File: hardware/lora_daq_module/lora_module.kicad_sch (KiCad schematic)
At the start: 28 parts, among them J2 SMA_Edge_50Ω, J3 USB_C_Receptacle_USB2.0_14P, J4 EXT_UART, J5 SWD, J6 Micro_SD_Card_Det1, U3 CP2102N-Axx-xQFN20, U4 Wio-E5_STM32WLE5JC, U5 CAT24C256

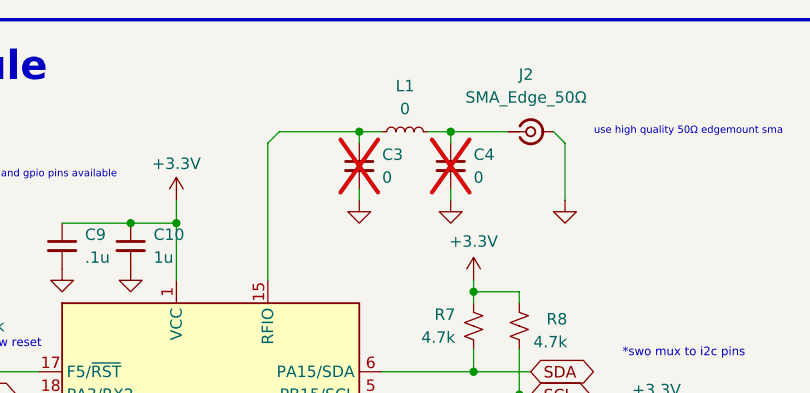
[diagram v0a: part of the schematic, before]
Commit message: assign parts and update BOM in symbol field table, warn: pcb footprints need update
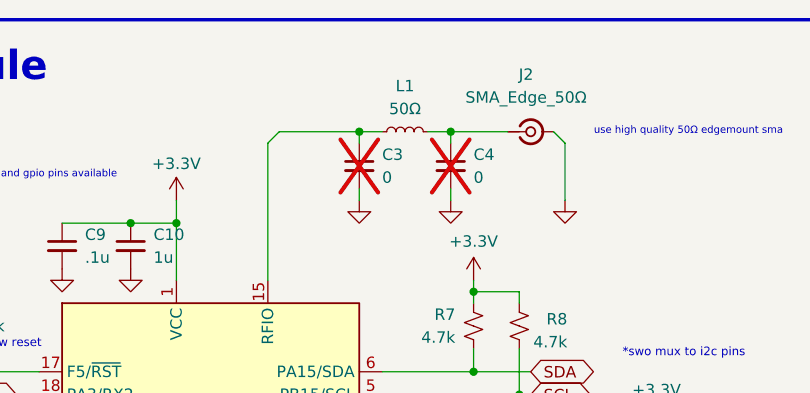
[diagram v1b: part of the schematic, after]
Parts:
- C10, C5: Desc (none) -> CAP CER 1UF 16V X7R 0603; Dist (none) -> Digikey; Dist PN (none) -> 490-5241-1-ND; Mfr (none) -> Murata Electronics; Mfr PN (none) -> GCM188R71C105KA64D
- C11, C13: Desc (none) -> CAP CER 10000PF 100V X7R 0603; Dist (none) -> Digikey; Dist PN (none) -> 490-4781-1-ND; Mfr (none) -> Murata Electronics; Mfr PN (none) -> GCM188R72A103KA37D
- C12, C6, C7, C9: Desc (none) -> CAP CER 0.1UF 16V X7R 0603; Dist (none) -> Digikey; Dist PN (none) -> 311-1088-1-ND; Mfr (none) -> YAGEO; Mfr PN (none) -> CC0603KRX7R7BB104
- D3: Desc (none) -> TVS DIODE 5.5VWM 8.5VC SOT1434; Dist (none) -> Digikey; Dist PN (none) -> F2715CT-ND; Mfr (none) -> Littelfuse Inc.; Mfr PN (none) -> SP0503BAHTG
- J2: Desc (none) -> SMA Connector Jack, Female Socket 50 Ohms Board Edge, End L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; Dist (none) -> Digkey; Dist PN (none) -> 900-0732511153-ND; Mfr (none) -> Molex; Mfr PN (none) -> 0732511153
- J3: Desc (none) -> CONN RCP USB3.1 TYPEC 24P SMD RA; Dist (none) -> Digikey; Dist PN (none) -> WM12856CT-ND; Mfr (none) -> Molex; Mfr PN (none) -> 1054500101
- J4: Desc (none) -> Connector Header Through Hole 3 position 0.098" (2.50mm); Dist (none) -> Digikey; Dist PN (none) -> 455-B3B-EH-A-ND; Mfr (none) -> JST Sales America Inc.; Mfr PN (none) -> B3B-EH-A
- J5: Desc (none) -> CONN HEADER VERT 6POS 2.54MM; Dist (none) -> Digikey; Dist PN (none) -> 732-5295-ND; Mfr (none) -> Würth Elektronik; Mfr PN (none) -> 61300621121
- J6: Desc (none) -> CONN MICRO SD CARD R/A SMD; Dist (none) -> Digikey; Dist PN (none) -> WM6357CT-ND; Mfr (none) -> Molex; Mfr PN (none) -> 1040310811
- L1: value 0 -> 50Ω; Desc (none) -> 50 Ohms ±0.1% 0.52W Chip Resistor 1206 (3216 Metric) Anti-S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; Dist (none) -> Digikey; Dist PN (none) -> 541-TNPW120650R0BEENCT-ND; Mfr (none) -> Vishay Dale; Mfr PN (none) -> TNPW120650R0BEEN
- R4, R5: Desc (none) -> 5.1 kOhms ±1% 0.1W, 1/10W Chip Resistor 0603 (1608 Metric) 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; Dist (none) -> Digikey; Dist PN (none) -> 311-5.10KHRCT-ND; Mfr (none) -> YAGEO; Mfr PN (none) -> RC0603FR-075K1L
- R6, R7, R8, R9: Desc (none) -> 4.7 kOhms ±5% 0.1W, 1/10W Chip Resistor 0603 (1608 Metric) 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; Dist (none) -> Digikey; Dist PN (none) -> 311-4.7KGRCT-ND; Mfr (none) -> YAGEO; Mfr PN (none) -> RC0603JR-074K7L
- TP1: now left out of the parts list
- U3: Desc (none) -> IC USB TO UART BRIDGE QFN20; Dist (none) -> Digikey; Dist PN (none) -> 336-5886-1-ND; Mfr (none) -> Silicon Labs; Mfr PN (none) -> CP2102N-A02-GQFN20R
- U4: Desc (none) -> RF TXRX MOD ISM<1GHZ SMD LORA; Dist (none) -> Digikey; Dist PN (none) -> 1597-317990829CT-ND; Mfr (none) -> Seeed Technology Co., Ltd; Mfr PN (none) -> 317990829
- U5: Desc (none) -> EEPROM Memory IC 256Kbit I2C 1 MHz 500 ns 8-SOIC; Dist (none) -> Digikey; Dist PN (none) -> CAT24C256WI-GT3OSCT-ND; Mfr (none) -> onsemi; Mfr PN (none) -> CAT24C256WI-GT3

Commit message: near-complete layout of power domain
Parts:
- J3: footprint Connector_USB:USB_C_Receptacle_Molex_105450-0101 -> Connector_USB:USB_C_Receptacle_GCT_USB4105-xx-A_16P_TopMnt_Horizontal; Desc CONN RCP USB3.1 TYPEC 24P SMD RA -> USB-C (USB TYPE-C) USB 2.0 Receptacle Connector 24 (16+8 Du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; Dist PN WM12856CT-ND -> 2073-USB4105-GF-A-120CT-ND; Mfr Molex -> GCT; Mfr PN 1054500101 -> USB4105-GF-A-120
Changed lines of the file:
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@@
 			)
 		)
-		(property "Footprint" "Connector_USB:USB_C_Receptacle_Molex_105450-0101"
+		(property "Footprint" "Connector_USB:USB_C_Receptacle_GCT_USB4105-xx-A_16P_TopMnt_Horizontal"
 			(at 39.37 54.61 0)
 			(effects
@@
 			)
 		)
-		(property "Desc" "CONN RCP USB3.1 TYPEC 24P SMD RA"
+		(property "Desc" "USB-C (USB TYPE-C) USB 2.0 Receptacle Connector 24 (16+8 Dummy) Position Surface Mount, Right Angle; Through Hole"
 			(at 35.56 54.61 0)
 			(effects
@@
 			)
 		)
-		(property "Dist PN" "WM12856CT-ND"
+		(property "Dist PN" "2073-USB4105-GF-A-120CT-ND"
 			(at 35.56 54.61 0)
 			(effects
@@
 			)
 		)
-		(property "Mfr" "Molex"
+		(property "Mfr" "GCT"
 			(at 35.56 54.61 0)
 			(effects
@@
 			)
 		)
-		(property "Mfr PN" "1054500101"
+		(property "Mfr PN" "USB4105-GF-A-120"
 			(at 35.56 54.61 0)
 			(effects

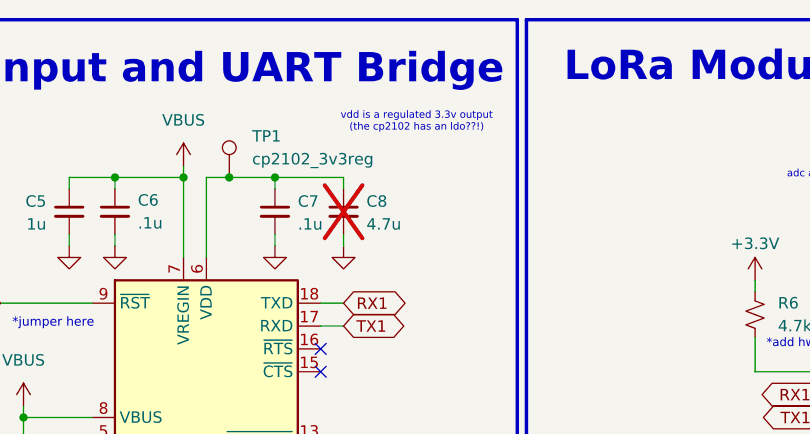
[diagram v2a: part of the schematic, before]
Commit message: lay traces to all components
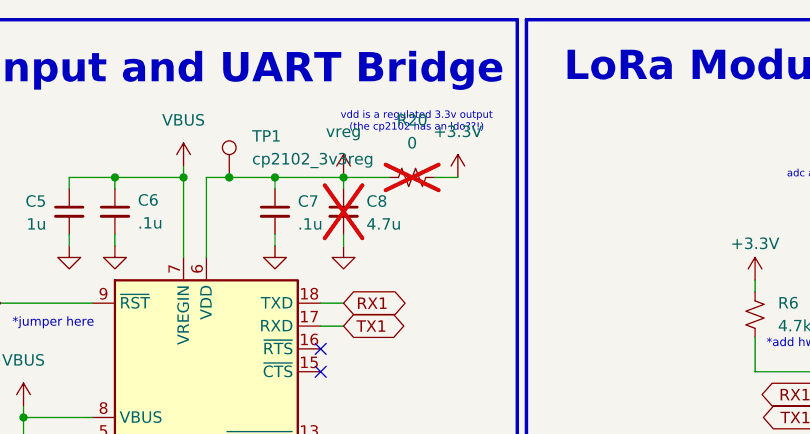
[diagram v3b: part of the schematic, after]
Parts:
- added R20: 0, Resistor_SMD:R_0603_1608Metric, symbol Device:R_Small_US
- TP1: footprint TestPoint:TestPoint_Pad_3.0x3.0mm -> TestPoint:TestPoint_Pad_1.5x1.5mm
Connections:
- net +3.3V: now also R20.2
- net vreg: now reaches C7.1, C8.1, TP1.1, U3.6 (VDD)
- net vreg: now also R20.1
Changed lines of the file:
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@@
 	)
 	(junction
+		(at 138.43 38.1)
+		(diameter 0)
+		(color 0 0 0 0)
+	)
+	(junction
 		(at 212.09 105.41)
 		(diameter 0)
@@
 	(wire
 		(pts
+			(xy 148.59 38.1) (xy 151.13 38.1)
+		)
+		(stroke
+			(width 0)
+			(type default)
+		)
+	)
+	(wire
+		(pts
 			(xy 105.41 67.31) (xy 110.49 67.31)
 		)
@@
 	(wire
 		(pts
+			(xy 138.43 38.1) (xy 143.51 38.1)
+		)
+		(stroke
+			(width 0)
+			(type default)
+		)
+	)
+	(wire
+		(pts
 			(xy 262.89 74.93) (xy 265.43 74.93)
 		)
@@
 	)
 	(symbol
+		(lib_id "power:+3.3V")
+		(at 151.13 38.1 0)
+		(unit 1)
+		(exclude_from_sim no)
+		(in_bom yes)
+		(on_board yes)
+		(dnp no)
+		(fields_autoplaced yes)
+		(property "Reference" "#PWR072"
+			(at 151.13 41.91 0)
+			(effects
+				(font
+					(size 1.27 1.27)
+				)
+				(hide yes)
+			)
+		)
+		(property "Value" "+3.3V"
+			(at 151.13 33.02 0)
+			(effects
+				(font
+					(size 1.27 1.27)
+				)
+			)
+		)
+		(property "Footprint" ""
+			(at 151.13 38.1 0)
+			(effects
+				(font
+					(size 1.27 1.27)
+				)
+				(hide yes)
+			)
+		)
+		(property "Datasheet" ""
+			(at 151.13 38.1 0)
+			(effects
+				(font
+					(size 1.27 1.27)
+				)
+				(hide yes)
+			)
+		)
+		(property "Description" "Power symbol creates a global label with name \"+3.3V\""
+			(at 151.13 38.1 0)
+			(effects
+				(font
+					(size 1.27 1.27)
+				)
+				(hide yes)
+			)
+		)
+		(pin "1"
+		)
+		(instances
+			(project ""
+				(path "/3a75d17e-6505-4097-95c7-feffd430343e/b2d61906-71c1-4ea1-893f-6962d616acd4"
+					(reference "#PWR072")
+					(unit 1)
+				)
+			)
+		)
+	)
+	(symbol
 		(lib_id "power:GND")
 		(at 71.12 52.07 0)
@@
 	)
 	(symbol
+		(lib_id "Device:R_Small_US")
+		(at 146.05 38.1 90)
+		(unit 1)
+		(exclude_from_sim no)
+		(in_bom yes)
+		(on_board yes)
+		(dnp yes)
+		(fields_autoplaced yes)
+		(property "Reference" "R20"
+			(at 146.05 31.75 90)
+			(effects
+				(font
+					(size 1.27 1.27)
+				)
+			)
+		)
+		(property "Value" "0"
+			(at 146.05 34.29 90)
+			(effects
+				(font
+					(size 1.27 1.27)
+				)
+			)
+		)
+		(property "Footprint" "Resistor_SMD:R_0603_1608Metric"
+			(at 146.05 38.1 0)
+			(effects
+				(font
+					(size 1.27 1.27)
+				)
+				(hide yes)
+			)
+		)
+		(property "Datasheet" "~"
+			(at 146.05 38.1 0)
+			(effects
+				(font
+					(size 1.27 1.27)
+				)
+				(hide yes)
+			)
+		)
+		(property "Description" "Resistor, small US symbol"
+			(at 146.05 38.1 0)
+			(effects
+				(font
+					(size 1.27 1.27)
+				)
+				(hide yes)
+			)
+		)
+		(pin "2"
+		)
+		(pin "1"
+		)
+		(instances
+			(project ""
+				(path "/3a75d17e-6505-4097-95c7-feffd430343e/b2d61906-71c1-4ea1-893f-6962d616acd4"
+					(reference "R20")
+					(unit 1)
+				)
+			)
+		)
+	)
+	(symbol
 		(lib_id "Device:C_Small")
 		(at 196.85 45.72 0)
@@
 			)
 		)
-		(property "Footprint" "TestPoint:TestPoint_Pad_3.0x3.0mm"
+		(property "Footprint" "TestPoint:TestPoint_Pad_1.5x1.5mm"
 			(at 130.81 38.1 0)
 			(effects
@@
 					(unit 1)
 				)
+			)
+		)
+	)
+	(symbol
+		(lib_id "power:VBUS")
+		(at 138.43 38.1 0)
+		(unit 1)
+		(exclude_from_sim no)
+		(in_bom yes)
+		(on_board yes)
+		(dnp no)
+		(fields_autoplaced yes)
+		(property "Reference" "#PWR071"
+			(at 138.43 41.91 0)
+			(effects
+				(font
+					(size 1.27 1.27)
+				)
+				(hide yes)
+			)
+		)
+		(property "Value" "vreg"
+			(at 138.43 33.02 0)
+			(effects
+				(font
+					(size 1.27 1.27)
+				)
+			)
+		)
+		(property "Footprint" ""
+			(at 138.43 38.1 0)
+			(effects
+				(font
+					(size 1.27 1.27)
+				)
+				(hide yes)
+			)
+		)
+		(property "Datasheet" ""
+			(at 138.43 38.1 0)
+			(effects
+				(font
+					(size 1.27 1.27)
+				)
+				(hide yes)
+			)
+		)
+		(property "Description" "Power symbol creates a global label with name \"VBUS\""
+			(at 138.43 38.1 0)
+			(effects
+				(font
+					(size 1.27 1.27)
+				)
+				(hide yes)
+			)
+		)
+		(pin "1"
+		)
+		(instances
+			(project "lora_daq_module"
+				(path "/3a75d17e-6505-4097-95c7-feffd430343e/b2d61906-71c1-4ea1-893f-6962d616acd4"
+					(reference "#PWR071")
+					(unit 1)
+				)

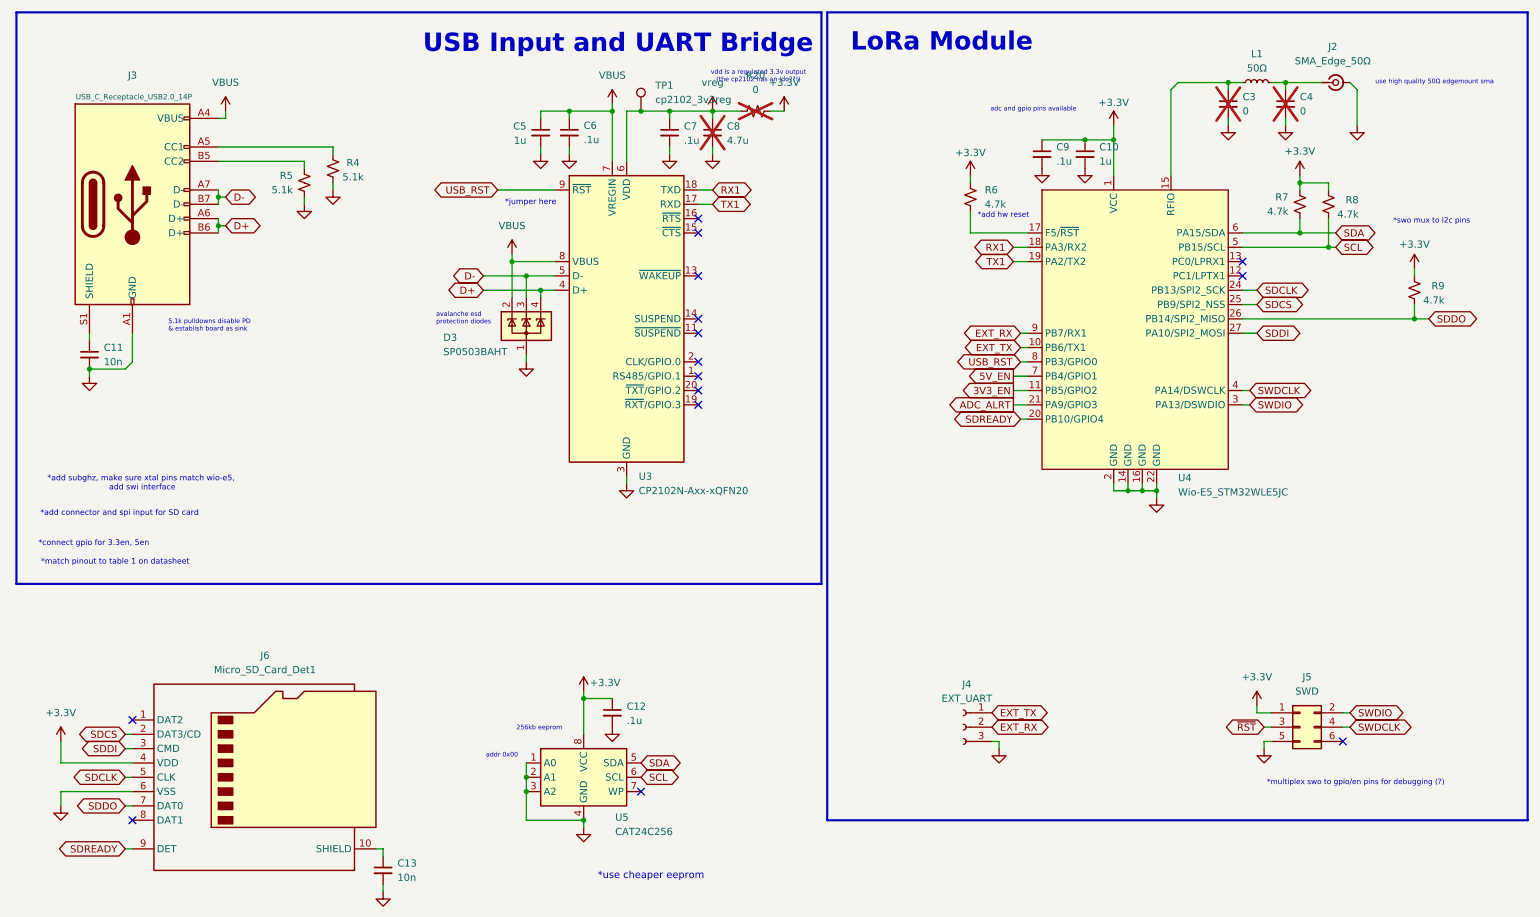
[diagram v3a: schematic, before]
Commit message: add test points and antenna microstrip
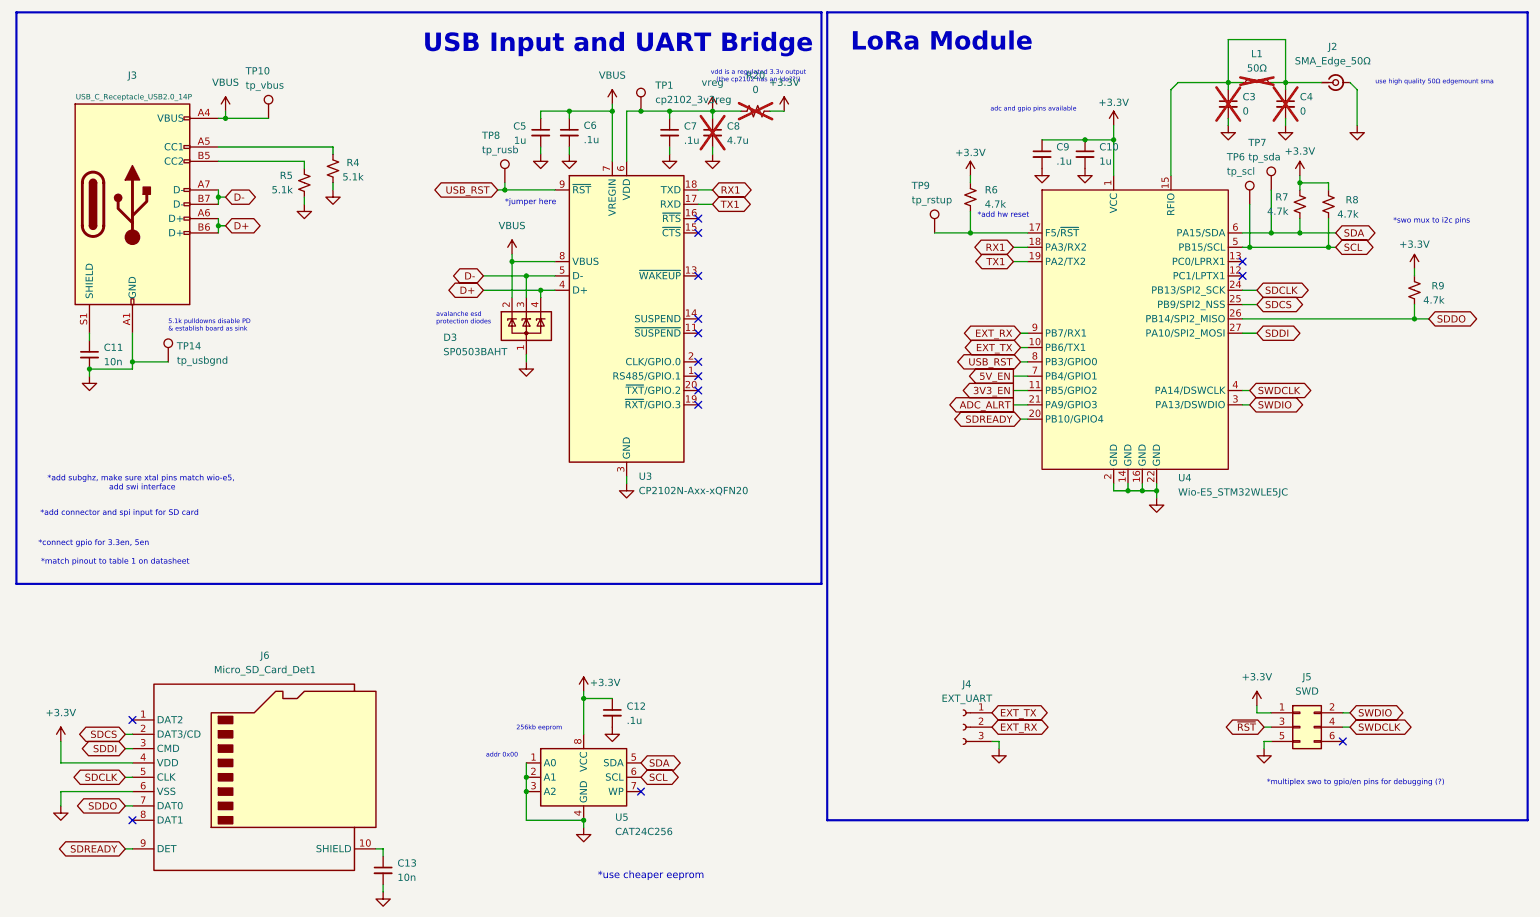
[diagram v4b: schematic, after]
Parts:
- added TP10: tp_vbus, TestPoint:TestPoint_THTPad_1.5x1.5mm_Drill0.7mm, symbol Connector:TestPoint
- added TP14: tp_usbgnd, TestPoint:TestPoint_THTPad_1.5x1.5mm_Drill0.7mm, symbol Connector:TestPoint
- added TP6: tp_scl, TestPoint:TestPoint_THTPad_1.5x1.5mm_Drill0.7mm, symbol Connector:TestPoint
- added TP7: tp_sda, TestPoint:TestPoint_THTPad_1.5x1.5mm_Drill0.7mm, symbol Connector:TestPoint
- added TP8: tp_rusb, TestPoint:TestPoint_THTPad_1.5x1.5mm_Drill0.7mm, symbol Connector:TestPoint
- added TP9: tp_rstup, TestPoint:TestPoint_THTPad_1.5x1.5mm_Drill0.7mm, symbol Connector:TestPoint
- C3, C4: now left out of the parts list
- L1: now not fitted; now left out of the parts list
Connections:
- net GND: now also TP14.1
- net SCL: now also TP6.1
- net SDA: now also TP7.1
- net USB_RST: now also TP8.1
- net VBUS: now also TP10.1
- net at C4.1, J2.1 (In), L1.2: now also C3.1, L1.1, U4.15 (RFIO)
- net at R6.2, U4.17 (F5/~{RST}): now also TP9.1
